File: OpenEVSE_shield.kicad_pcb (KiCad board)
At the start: 2 copper layers, 100.3 x 53.6 mm, 78 parts, among them J1 COMMS, J10 LCD, J11 PSU, J12 PILOT, J13 MAINS, J14 GFCI_TEST, J2 Conn_01x06, J3 Conn_01x08, J4 Conn_01x08, J5 Conn_01x08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

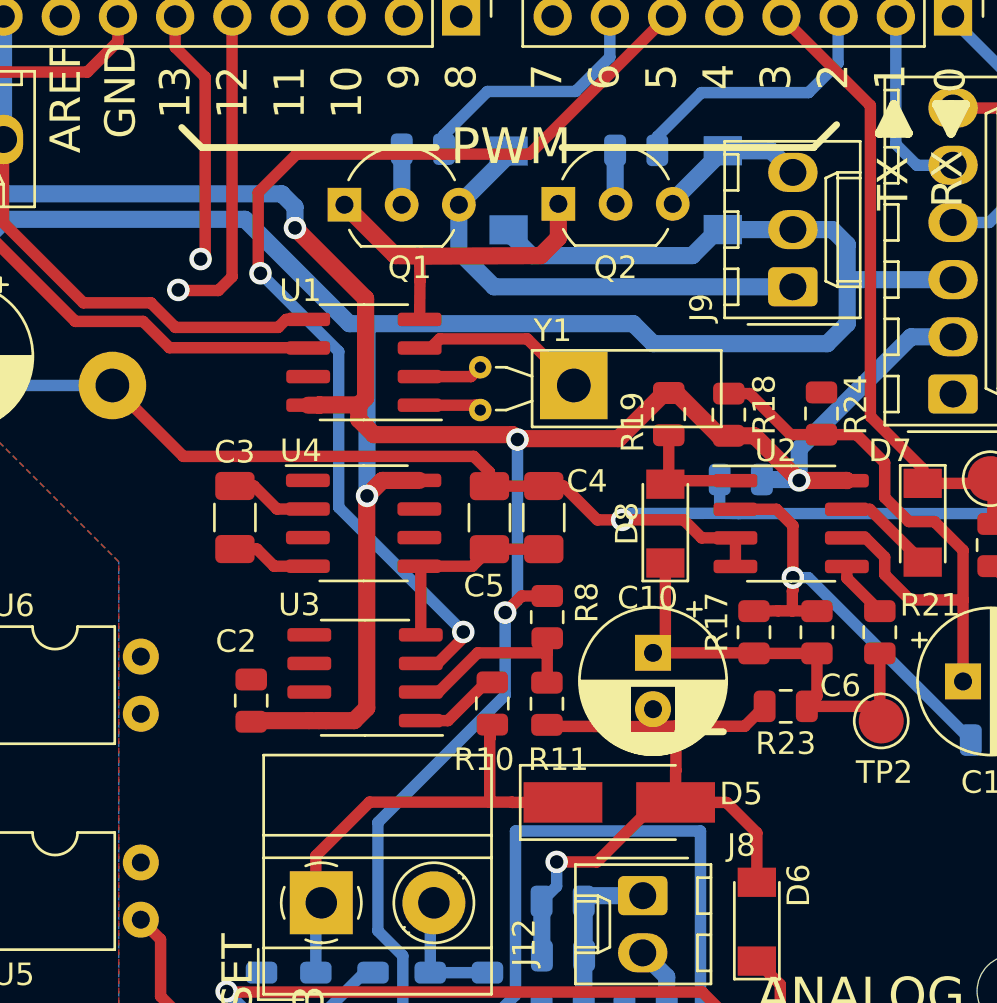
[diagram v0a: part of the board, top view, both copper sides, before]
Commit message: fix: Add missing optocouplers connections on PCB
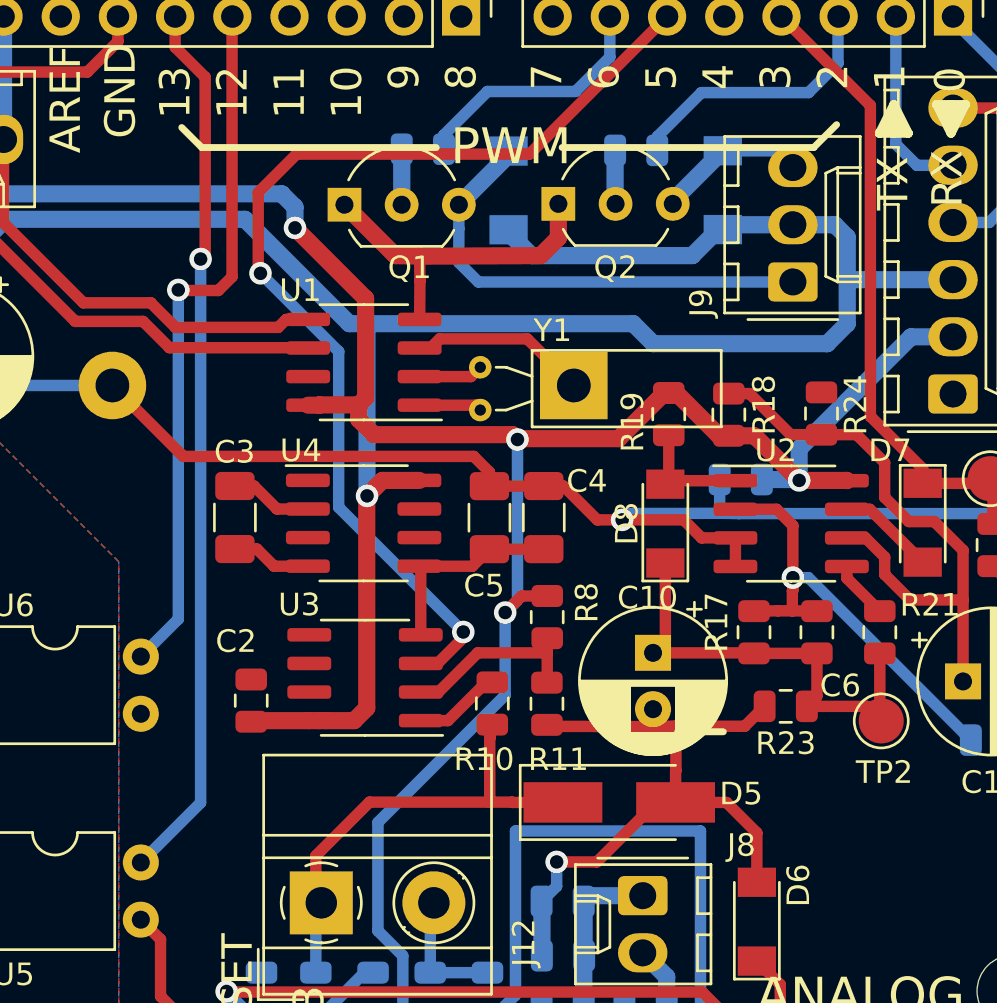
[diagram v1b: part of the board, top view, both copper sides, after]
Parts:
- moved J9 0.22 mm to (153.4, 92.6)
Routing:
- net /AC_TEST_L2: track 11.4 -> 39.3 mm
- net /AC_TEST_L1: track 14.2 -> 31.2 mm
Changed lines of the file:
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@@
     (thickness 1.6)
     (drawings 79)
-    (tracks 439)
+    (tracks 445)
     (zones 0)
     (modules 78)
@@
   )
   (module Connector_Molex:Molex_KK-254_AE-6410-03A_1x03_P2.54mm_Vertical (layer Top)
-    (at 153.416 92.7735 90)
+    (at 153.416 92.5576 90)
     (descr "Molex KK-254 Interconnect System, old/engineering part number: AE-6410-03A example for new part number: 22-27-2031, 3 Pins (http://www.molex.com/pdm_docs/sd/022272021_sd.pdf), generated with kicad-footprint-generator")
     (tags "connector Molex KK-254 side entry")
@@
   (segment (start 135.6106 126.7206) (end 127.7747 126.7206) (width 0.508) (layer Top) (net 2))
   (segment (start 137.922 129.032) (end 135.6106 126.7206) (width 0.508) (layer Top) (net 2))
-  (segment (start 153.416 90.2335) (end 150.3045 90.2335) (width 0.762) (layer Bottom) (net 3) (status 30))
   (segment (start 141.8082 91.3892) (end 140.7922 90.3732) (width 0.762) (layer Bottom) (net 3) (status 20))
   (segment (start 148.9488 91.3892) (end 141.8082 91.3892) (width 0.762) (layer Bottom) (net 3))
@@
   (segment (start 129.4107 112.0394) (end 129.3622 112.0879) (width 0.762) (layer Top) (net 3) (status 30))
   (segment (start 131.9418 112.0394) (end 129.4107 112.0394) (width 0.762) (layer Top) (net 3) (status 30))
-  (segment (start 155.1686 90.2335) (end 155.829 90.8939) (width 0.762) (layer Bottom) (net 3))
-  (segment (start 153.416 90.2335) (end 155.1686 90.2335) (width 0.762) (layer Bottom) (net 3) (status 10))
   (segment (start 160.528 92.456) (end 160.528 92.329) (width 0.762) (layer Bottom) (net 3) (status 30))
   (segment (start 160.528 92.456) (end 155.829 92.456) (width 0.762) (layer Bottom) (net 3) (status 10))
-  (segment (start 155.829 90.8939) (end 155.829 92.456) (width 0.762) (layer Bottom) (net 3))
   (segment (start 131.9418 112.0394) (end 132.3721 112.0394) (width 0.762) (layer Top) (net 3) (status 30))
   (segment (start 132.3721 112.0394) (end 132.680606 112.0394) (width 0.762) (layer Top) (net 3) (status 30))
@@
   (segment (start 118.4529 89.7763) (end 129.0828 89.7763) (width 0.762) (layer Bottom) (net 3))
   (segment (start 116.3955 94.615) (end 116.3955 91.8337) (width 0.762) (layer Bottom) (net 3) (status 10))
+  (segment (start 155.278 90.0176) (end 153.416 90.0176) (width 0.762) (layer Bottom) (net 3))
+  (segment (start 155.829 90.5686) (end 155.278 90.0176) (width 0.762) (layer Bottom) (net 3))
+  (segment (start 155.829 92.456) (end 155.829 90.5686) (width 0.762) (layer Bottom) (net 3))
+  (segment (start 150.5204 90.0176) (end 150.3045 90.2335) (width 0.762) (layer Bottom) (net 3))
+  (segment (start 153.416 90.0176) (end 150.5204 90.0176) (width 0.762) (layer Bottom) (net 3))
   (segment (start 103.9495 127.2921) (end 102.6414 127.2921) (width 0.762) (layer Bottom) (net 4))
   (segment (start 106.553 124.6886) (end 103.9495 127.2921) (width 0.762) (layer Bottom) (net 4))
@@
   (segment (start 126.1491 92.9386) (end 127.9017 92.9386) (width 0.508) (layer Top) (net 18))
   (segment (start 126.1237 92.9132) (end 126.1491 92.9386) (width 0.508) (layer Top) (net 18))
+  (segment (start 126.1237 107.5309) (end 124.46 109.1946) (width 0.508) (layer Bottom) (net 18))
+  (segment (start 126.1237 92.9132) (end 126.1237 107.5309) (width 0.508) (layer Bottom) (net 18))
   (segment (start 125.984 82.1309) (end 125.984 80.772) (width 0.508) (layer Top) (net 19) (status 20))
   (segment (start 127.3175 83.4644) (end 125.984 82.1309) (width 0.508) (layer Top) (net 19))
@@
   (segment (start 127.3175 91.3384) (end 127.1143 91.5416) (width 0.508) (layer Top) (net 19))
   (segment (start 127.1143 91.5416) (end 127.127 91.5416) (width 0.508) (layer Bottom) (net 19))
+  (segment (start 127.1143 115.6843) (end 124.46 118.3386) (width 0.508) (layer Bottom) (net 19))
+  (segment (start 127.1143 91.5416) (end 127.1143 115.6843) (width 0.508) (layer Bottom) (net 19))
   (segment (start 137.3124 123.2304) (end 137.3124 119.8499) (width 0.508) (layer Bottom) (net 20) (status 30))
   (segment (start 137.3124 123.2304) (end 139.8524 123.2304) (width 0.508) (layer Bottom) (net 20) (status 30))
@@
   (segment (start 111.493 111.0996) (end 111.493 107.5306) (width 0.762) (layer Bottom) (net 69))
   (segment (start 167.386 108.077) (end 167.386 110.49) (width 0.508) (layer Bottom) (net 70) (status 30))
-  (segment (start 140.7922 86.9188) (end 138.5824 89.1286) (width 0.762) (layer Bottom) (net 71) (status 30))
+  (segment (start 138.5824 90.18926) (end 138.5824 89.1286) (width 0.508) (layer Bottom) (net 71))
+  (segment (start 138.5824 91.694) (end 138.5824 90.18926) (width 0.508) (layer Bottom) (net 71))
+  (segment (start 139.446 92.5576) (end 138.5824 91.694) (width 0.508) (layer Bottom) (net 71))
+  (segment (start 153.416 92.5576) (end 139.446 92.5576) (width 0.508) (layer Bottom) (net 71))
   (segment (start 140.7922 86.7436) (end 140.7922 86.9188) (width 0.762) (layer Bottom) (net 71) (status 30))
-  (segment (start 138.5824 91.2114) (end 138.5824 89.1286) (width 0.762) (layer Bottom) (net 71) (status 20))
-  (segment (start 140.1445 92.7735) (end 138.5824 91.2114) (width 0.762) (layer Bottom) (net 71))
-  (segment (start 153.416 92.7735) (end 140.1445 92.7735) (width 0.762) (layer Bottom) (net 71) (status 10))
+  (segment (start 140.7922 86.9188) (end 138.5824 89.1286) (width 0.762) (layer Bottom) (net 71) (status 30))
   (segment (start 148.082 88.956) (end 150.3045 86.7335) (width 0.762) (layer Bottom) (net 72) (status 30))
   (segment (start 148.082 89.0905) (end 148.082 88.956) (width 0.762) (layer Bottom) (net 72) (status 30))
-  (segment (start 152.456 86.7335) (end 153.416 87.6935) (width 0.762) (layer Bottom) (net 72) (status 20))
-  (segment (start 150.3045 86.7335) (end 152.456 86.7335) (width 0.762) (layer Bottom) (net 72) (status 10))
+  (segment (start 152.6719 86.7335) (end 153.416 87.4776) (width 0.508) (layer Bottom) (net 72))
+  (segment (start 150.3045 86.7335) (end 152.6719 86.7335) (width 0.508) (layer Bottom) (net 72))
   (segment (start 156.8349 102.6541) (end 159.1818 105.001) (width 0.508) (layer Top) (net 73) (status 20))
   (segment (start 155.8148 102.6541) (end 156.8349 102.6541) (width 0.508) (layer Top) (net 73) (status 10))

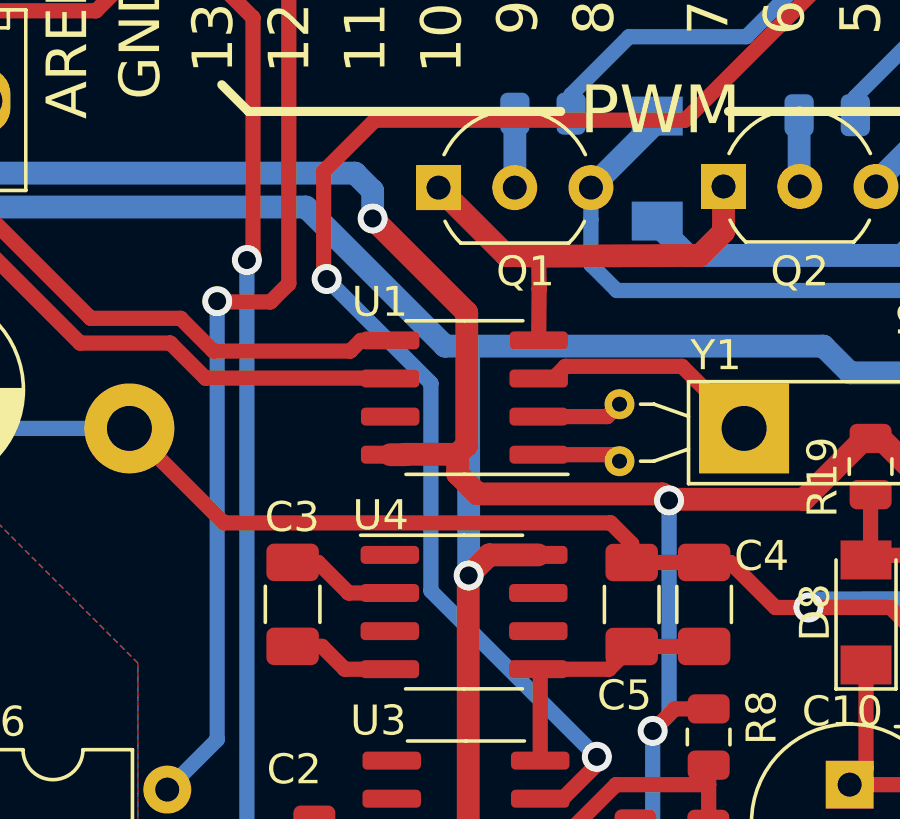
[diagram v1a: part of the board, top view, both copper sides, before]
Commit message: fix: missing GND connection at ICL7660
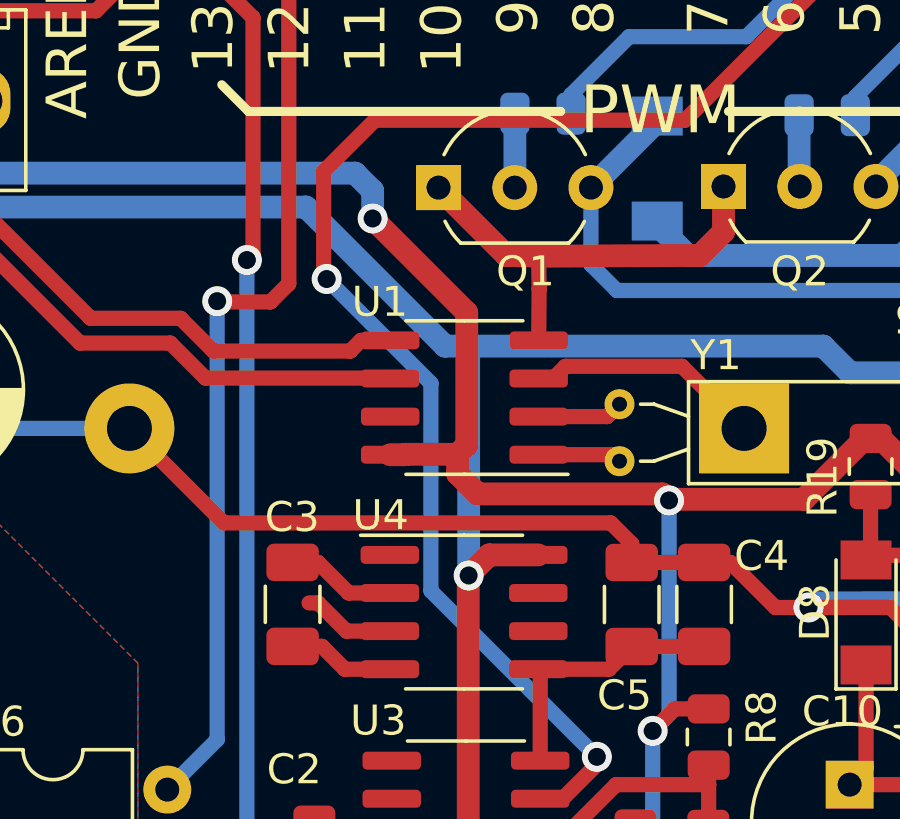
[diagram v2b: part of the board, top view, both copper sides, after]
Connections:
- U4 pad 3: Net-(U4-Pad3) -> GND
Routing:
- net GND: track 222.1 -> 225.1 mm

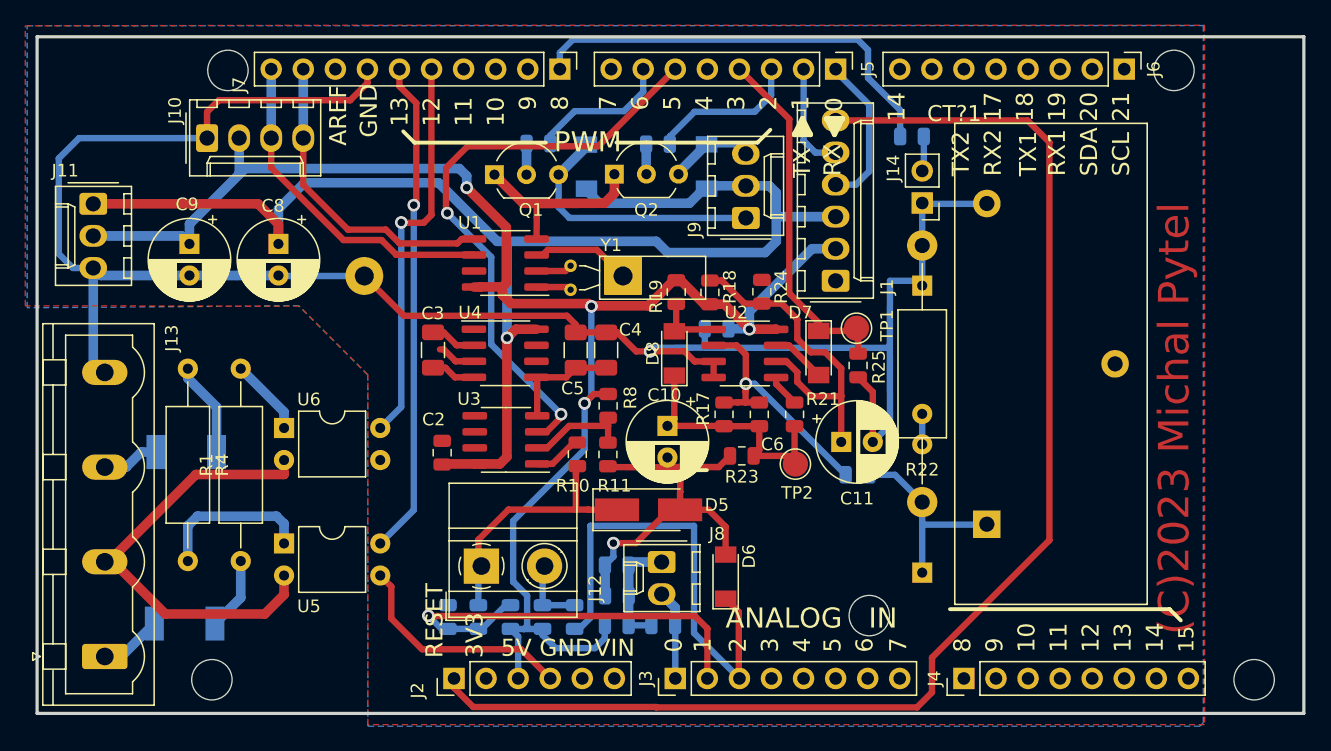
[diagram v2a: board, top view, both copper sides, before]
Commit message: fix DRC errors, align overlay colliding with soldering pads
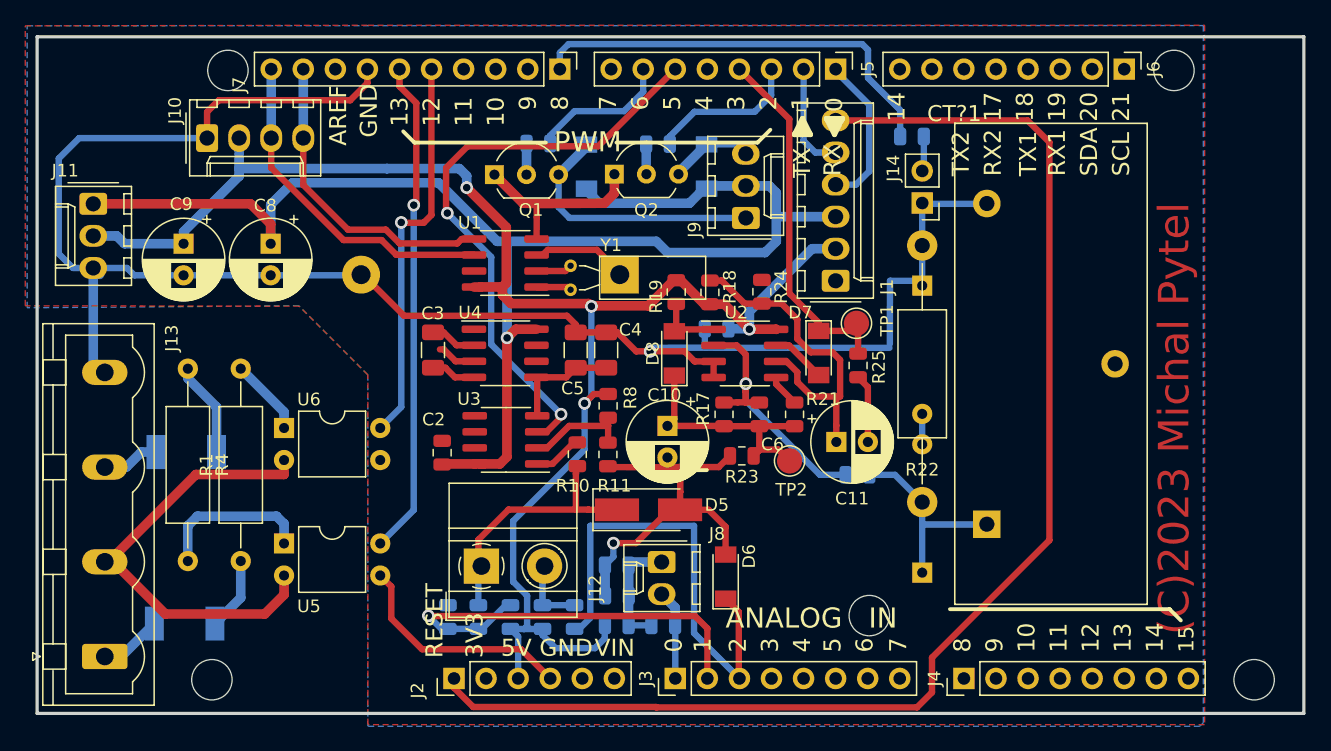
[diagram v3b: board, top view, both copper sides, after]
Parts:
- moved C8 0.61 mm to (115.8, 94.6)
- moved TP2 0.52 mm to (156.9, 111.8)
- moved C9 0.47 mm to (108.9, 94.6)
- moved TP1 0.39 mm to (162.2, 100.9)
- moved C11 0.39 mm to (160.6, 110.3)
- moved BT1 0.28 mm to (143.4, 97.1)
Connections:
- net /AC_RELAY_1 renamed Net-(J7-Pad4)
- net Net-(C4-Pad1) renamed -12V
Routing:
- net GND: track 225.1 -> 216.4 mm
- net /GFCI_INT: track 29.3 -> 30.3 mm
- net Net-(C10-Pad1): track 20.6 -> 19.7 mm
- net Net-(C6-Pad1): track 20.3 -> 21.1 mm

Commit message: Tweak values during assembly and testing
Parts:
- C6: value 0.1u -> 100n
- R16: value 330 -> 470
- R17: value 40k -> 470k
- R19: value 10k -> 22k
- R2: value 22 -> 33
- R22: value 100 -> 500
- R23: value 100k -> NOT FITTED
- R24: value 2k2 -> 8k2
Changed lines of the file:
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@@
       (effects (font (size 1 1) (thickness 0.15)))
     )
-    (fp_text value 0.1u (at 0 1.65 90) (layer F.Fab)
+    (fp_text value 100n (at 0 1.65 90) (layer F.Fab)
       (effects (font (size 1 1) (thickness 0.15)))
     )
@@
       (effects (font (size 1 1) (thickness 0.15)))
     )
-    (fp_text value 100 (at 10.16 2.92 90) (layer F.Fab)
+    (fp_text value 500 (at 10.16 2.92 90) (layer F.Fab)
       (effects (font (size 1 1) (thickness 0.15)))
     )
@@
       (effects (font (size 1 1) (thickness 0.15)))
     )
-    (fp_text value 2k2 (at 0 1.65 90) (layer F.Fab)
+    (fp_text value 8k2 (at 0 1.65 90) (layer F.Fab)
       (effects (font (size 1 1) (thickness 0.15)))
     )
@@
       (effects (font (size 1 1) (thickness 0.15)))
     )
-    (fp_text value 100k (at 0 1.65) (layer F.Fab)
+    (fp_text value "NOT FITTED" (at 0 1.65) (layer F.Fab)
       (effects (font (size 1 1) (thickness 0.15)))
     )
@@
       (effects (font (size 1 1) (thickness 0.15)))
     )
-    (fp_text value 10k (at 0 1.65 90) (layer F.Fab)
+    (fp_text value 22k (at 0 1.65 90) (layer F.Fab)
       (effects (font (size 1 1) (thickness 0.15)))
     )
@@
       (effects (font (size 1 1) (thickness 0.15)))
     )
-    (fp_text value 40k (at 0 1.65 90) (layer F.Fab)
+    (fp_text value 470k (at 0 1.65 90) (layer F.Fab)
       (effects (font (size 1 1) (thickness 0.15)))
     )
@@
       (effects (font (size 1 1) (thickness 0.15)) (justify mirror))
     )
-    (fp_text value 330 (at 0 -1.65) (layer B.Fab)
+    (fp_text value 470 (at 0 -1.65) (layer B.Fab)
       (effects (font (size 1 1) (thickness 0.15)) (justify mirror))
     )
@@
       (effects (font (size 1 1) (thickness 0.15)) (justify mirror))
     )
-    (fp_text value 22 (at 0 -1.65 180) (layer B.Fab)
+    (fp_text value 33 (at 0 -1.65 180) (layer B.Fab)
       (effects (font (size 1 1) (thickness 0.15)) (justify mirror))
     )
@@
   (segment (start 131.8783 102.6414) (end 130.5052 102.6414) (width 0.508) (layer Top) (net 63) (status 10))
   (segment (start 130.5052 102.6414) (end 129.4832 101.6194) (width 0.508) (layer Top) (net 63) (status 20))
-  (segment (start 136.8918 105.2449) (end 136.8283 105.1814) (width 0.508) (layer Top) (net 83) (status 30))
-  (segment (start 136.8918 108.2294) (end 136.8918 105.2449) (width 0.508) (layer Top) (net 83) (status 30))
-  (segment (start 139.1853 105.1814) (end 139.9413 104.4254) (width 0.508) (layer Top) (net 83) (status 20))
-  (segment (start 136.8283 105.1814) (end 139.1853 105.1814) (width 0.508) (layer Top) (net 83) (status 10))
-  (segment (start 142.3513 104.4254) (end 142.3543 104.4224) (width 0.508) (layer Top) (net 83) (status 30))
-  (segment (start 139.9413 104.4254) (end 142.3513 104.4254) (width 0.508) (layer Top) (net 83) (status 30))
   (segment (start 157.2768 111.9886) (end 157.3403 112.0521) (width 0.508) (layer Top) (net 64) (status 30))
   (segment (start 147.7518 108.4834) (end 147.2057 109.0295) (width 0.508) (layer Top) (net 64) (status 30))
@@
   (segment (start 165.227 112.903) (end 167.386 115.062) (width 0.508) (layer Bottom) (net 82) (status 20))
   (segment (start 163.1927 112.903) (end 165.227 112.903) (width 0.508) (layer Bottom) (net 82) (status 10))
+  (segment (start 136.8918 105.2449) (end 136.8283 105.1814) (width 0.508) (layer Top) (net 83) (status 30))
+  (segment (start 136.8918 108.2294) (end 136.8918 105.2449) (width 0.508) (layer Top) (net 83) (status 30))
+  (segment (start 139.1853 105.1814) (end 139.9413 104.4254) (width 0.508) (layer Top) (net 83) (status 20))
+  (segment (start 136.8283 105.1814) (end 139.1853 105.1814) (width 0.508) (layer Top) (net 83) (status 10))
+  (segment (start 142.3513 104.4254) (end 142.3543 104.4224) (width 0.508) (layer Top) (net 83) (status 30))
+  (segment (start 139.9413 104.4254) (end 142.3513 104.4254) (width 0.508) (layer Top) (net 83) (status 30))
   (zone (net 2) (net_name GND) (layer Top) (hatch edge 0.508)
     (priority 6)
